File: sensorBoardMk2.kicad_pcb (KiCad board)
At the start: 2 copper layers, 47 parts, among them J1 B4B-PH-SM4-TB, J2 B4B-PH-SM4-TB, J3 B2B-PH-SM4-TB, J4 B2B-PH-SM4-TB, P1 TP, P2 TP, P3 TP, P4 TP, U1 SHT45, U2 BME280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

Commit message: Reworked schema
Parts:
- moved R5 2.97 mm to (91.2, 83.4)
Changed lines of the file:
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@@
 	(footprint "Resistor_SMD:R_0805_2012Metric_Pad1.20x1.40mm_HandSolder"
 		(layer "F.Cu")
-		(at 92.2 80.6)
+		(at 91.2 83.4)
 		(descr "Resistor SMD 0805 (2012 Metric), square (rectangular) end terminal, IPC-7351 nominal with elongated pad for handsoldering. (Body size source: IPC-SM-782 page 72, https://www.pcb-3d.com/wordpress/wp-content/uploads/ipc-sm-782a_amendment_1_and_2.pdf), generated with kicad-footprint-generator")
 		(tags "resistor handsolder")
@@
 		)
 		(fp_text user "${REFERENCE}"
-			(at 0 0 0)
+			(at -0.8 1.2 0)
 			(layer "F.Fab")
 			(effects

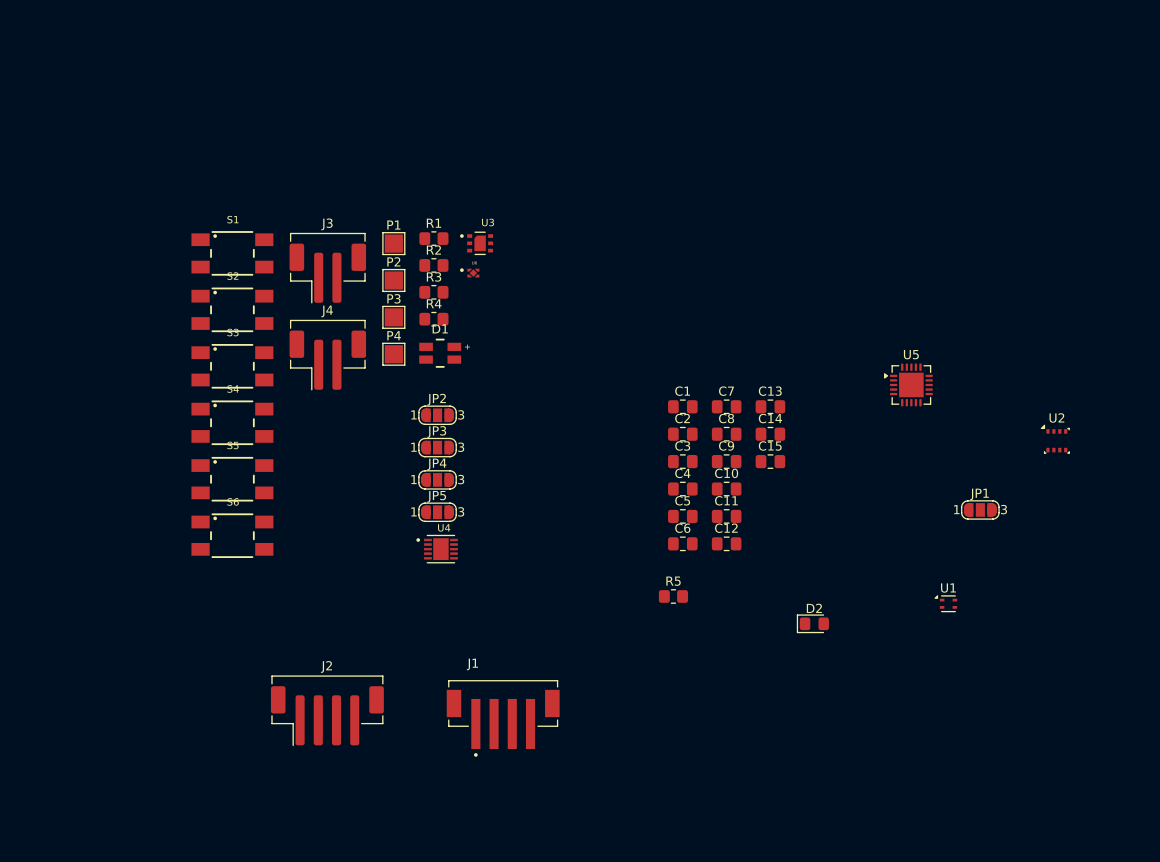
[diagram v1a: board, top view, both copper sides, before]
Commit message: Created pcb from schematic
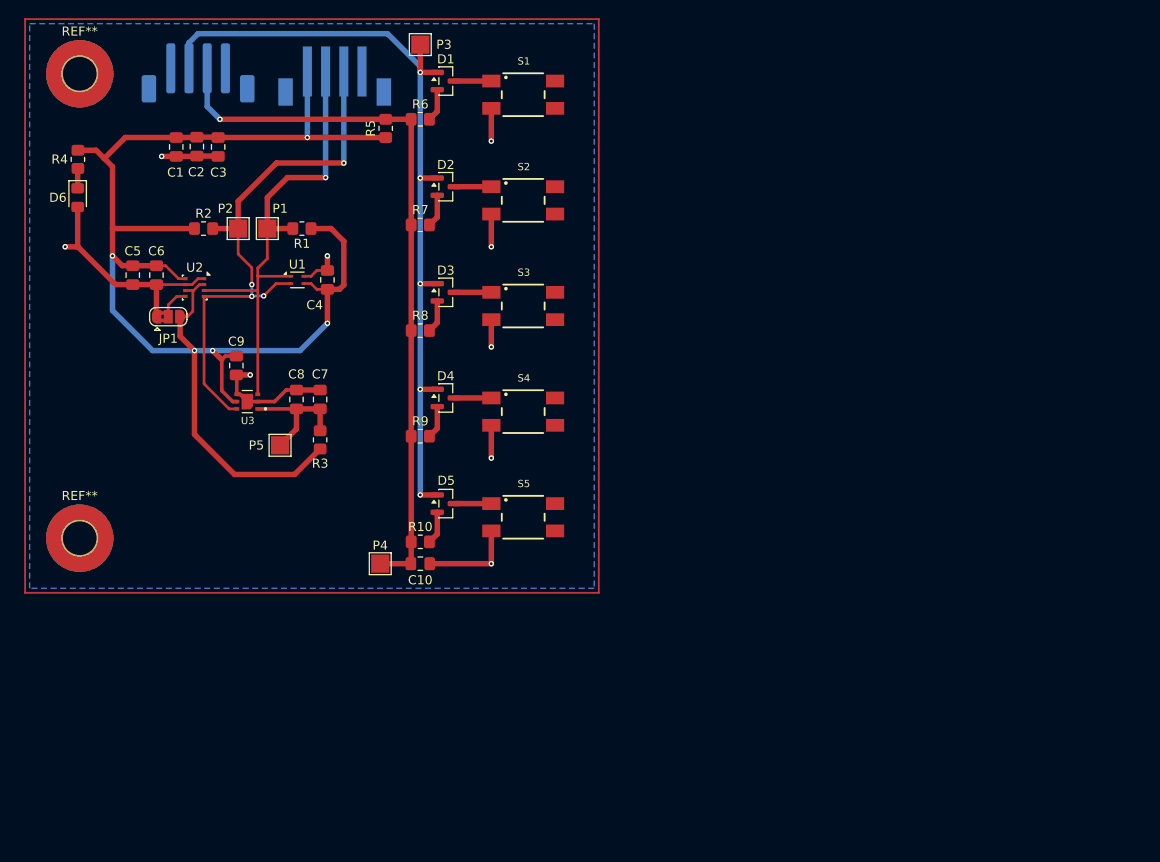
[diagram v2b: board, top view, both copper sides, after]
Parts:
- removed C11, C12, C14, C15: 1uF, Capacitor_SMD:C_0805_2012Metric_Pad1.18x1.45mm_HandSolder
- removed C13: 100nF, Capacitor_SMD:C_0805_2012Metric_Pad1.18x1.45mm_HandSolder
- removed J3, J4: B2B-PH-SM4-TB, Connector_JST:JST_PH_B2B-PH-SM4-TB_1x02-1MP_P2.00mm_Vertical
- removed JP2, JP3, JP4, JP5: SolderJumper_3_Bridged12, Jumper:SolderJumper-3_P1.3mm_Open_RoundedPad1.0x1.5mm_NumberLabels
- removed S6: 430181038816, sensorBoardMk2Library:430181038816
- removed U4: IS31FL3193-DLS2-TR, sensorBoardMk2Library:SON50P300X300X80-11N
- removed U5: MCP23008-xML, Package_DFN_QFN:QFN-20-1EP_4x4mm_P0.5mm_EP2.7x2.7mm
- removed U6: TPS7A0233PDQNR, sensorBoardMk2Library:IC_TPS7A0233PDQNR
- added D3: BAV70, Package_TO_SOT_SMD:SOT-23, F.Cu at (66.2, 50.0)
- added D4: BAV70, Package_TO_SOT_SMD:SOT-23, F.Cu at (66.2, 61.6)
- added D5: BAV70, Package_TO_SOT_SMD:SOT-23, F.Cu at (66.2, 73.2)
- added D6: LED_BLUE, LED_SMD:LED_0805_2012Metric_Pad1.15x1.40mm_HandSolder, F.Cu at (25.8, 39.6)
- added P5: TP, TestPoint:TestPoint_Pad_2.0x2.0mm, F.Cu at (48.0, 66.8)
- added R10: 56k, Resistor_SMD:R_0805_2012Metric_Pad1.20x1.40mm_HandSolder, F.Cu at (63.4, 77.4)
- added R6: 2.7k, Resistor_SMD:R_0805_2012Metric_Pad1.20x1.40mm_HandSolder, F.Cu at (63.4, 31.0)
- added R7: 5.6k, Resistor_SMD:R_0805_2012Metric_Pad1.20x1.40mm_HandSolder, F.Cu at (63.4, 42.6)
- added R8: 12k, Resistor_SMD:R_0805_2012Metric_Pad1.20x1.40mm_HandSolder, F.Cu at (63.4, 54.2)
- added R9: 22k, Resistor_SMD:R_0805_2012Metric_Pad1.20x1.40mm_HandSolder, F.Cu at (63.4, 65.8)
- added REF**: MountingHole_3.7mm_Pad_TopBottom, MountingHole:MountingHole_3.7mm_Pad_TopBottom, F.Cu at (26.0, 26.0)
- added REF**: MountingHole_3.7mm_Pad_TopBottom, MountingHole:MountingHole_3.7mm_Pad_TopBottom, F.Cu at (26.0, 77.0)
- D1: value WL-SFTW_3528_PLCC4 -> BAV70; footprint sensorBoardMk2Library:WL-SFTW_3528_PLCC4 -> Package_TO_SOT_SMD:SOT-23
- D2: value LED_RED -> BAV70; footprint LED_SMD:LED_0805_2012Metric_Pad1.15x1.40mm_HandSolder -> Package_TO_SOT_SMD:SOT-23
- J1, J2: moved to B.Cu
- JP1: footprint Jumper:SolderJumper-3_P1.3mm_Open_RoundedPad1.0x1.5mm_NumberLabels -> Jumper:SolderJumper-3_P1.3mm_Bridged2Bar12_RoundedPad1.0x1.5mm
- R1, R2: value 10k -> 5.6k
- R4: value 10k -> 120
- R5: value 2.7k -> 100k
- moved U2 96.2 mm to (38.6, 49.5), turned to -90 degrees
- moved JP1 91.7 mm to (35.7, 52.7)
- moved U1 79.9 mm to (49.9, 48.6)
- moved J2 72.0 mm to (39.0, 25.9)
- moved J1 69.7 mm to (54.0, 28.0)
- moved C5 66.0 mm to (31.8, 48.1), turned to -90 degrees
- moved C6 64.9 mm to (34.4, 48.1), turned to -90 degrees
- moved D2 62.8 mm to (66.2, 38.4)
- moved C1 62.5 mm to (36.6, 34.0), turned to -90 degrees
- moved C2 62.0 mm to (38.9, 34.0), turned to -90 degrees
- moved C3 61.6 mm to (41.2, 34.0), turned to -90 degrees
- moved R5 60.3 mm to (59.6, 32.0), turned to 90 degrees
- moved C9 54.9 mm to (43.2, 58.0), turned to -90 degrees
- moved C8 47.4 mm to (49.8, 61.8), turned to 90 degrees
- moved C4 45.3 mm to (53.2, 48.6), turned to 90 degrees
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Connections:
- C10 pad 1: /3V3_AO -> /ADC
- D1 pad 1: +3.3V -> /INT
- D1 pad 3: Net-(U4-OUT2) -> Net-(D1-K)
- D2 pad 1: Net-(D2-A) -> /INT
- D2 pad 2: GND -> Net-(D2-A-Pad2)
- J2 pad 2: /INT1 -> /INT
- J2 pad 3: /INT2 -> /ADC
- P3 pad 1: /INT1 -> /INT
- P4 pad 1: /INT2 -> /ADC
- R4 pad 1: /3V3_AO -> +3.3V
- R4 pad 2: /INT2 -> Net-(D6-A)
- R5 pad 1: /GP2 -> +3.3V
- R5 pad 2: Net-(D2-A) -> /ADC
- S1 pad 1: /INT2 -> Net-(D1-K)
- S1 pad 3: unconnected-(S1-Pad3) -> GND
- S1 pad 4: GND -> unconnected-(S1-Pad4)
- S2 pad 1: /GP3 -> Net-(D2-K)
- S2 pad 3: unconnected-(S2-Pad3) -> GND
- S2 pad 4: Net-(S2-Pad4) -> unconnected-(S2-Pad4)
- S3 pad 1: /GP4 -> Net-(D3-K)
- S3 pad 3: Net-(S2-Pad4) -> GND
- S3 pad 4: Net-(S3-Pad4) -> unconnected-(S3-Pad4)
- S4 pad 1: /GP5 -> Net-(D4-K)
- S4 pad 3: Net-(S3-Pad4) -> GND
- S4 pad 4: Net-(S4-Pad4) -> unconnected-(S4-Pad4)
- S5 pad 1: /GP6 -> Net-(D5-K)
- S5 pad 3: Net-(S4-Pad4) -> GND
- S5 pad 4: Net-(S5-Pad4) -> unconnected-(S5-Pad4)
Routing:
- net +3.3V: track 0.00 -> 167.1 mm, vias 0 -> 5
- net /INT: track 0.00 -> 89.5 mm, vias 0 -> 5
- net /ADC: track 0.00 -> 79.4 mm, vias 0 -> 1
- net GND: track 0.00 -> 73.7 mm, vias 0 -> 9
- net /SCL: track 0.00 -> 61.7 mm, vias 0 -> 4
- net /SDA: track 0.00 -> 53.4 mm, vias 0 -> 1
- net Net-(U3-VDD): track 0.00 -> 14.0 mm
- net Net-(D5-K): track 0.00 -> 4.06 mm
- net Net-(D4-K): track 0.00 -> 4.06 mm
- net Net-(D3-K): track 0.00 -> 4.06 mm
- net Net-(D2-K): track 0.00 -> 4.06 mm
- net Net-(D1-K): track 0.00 -> 4.06 mm
- net Net-(D4-A-Pad2): track 0.00 -> 3.62 mm
- net Net-(D1-A-Pad2): track 0.00 -> 3.62 mm
- net Net-(D3-A-Pad2): track 0.00 -> 3.62 mm
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- added copper zone on B.Cu, net GND

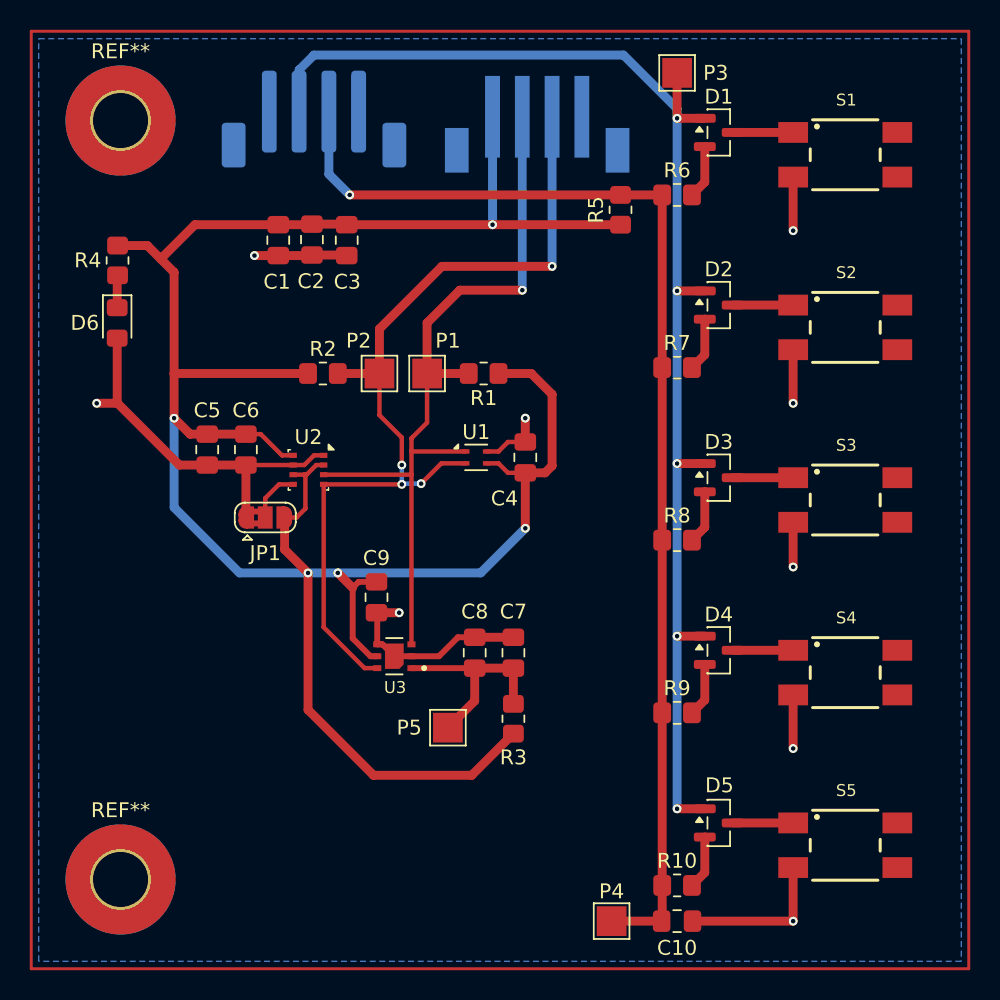
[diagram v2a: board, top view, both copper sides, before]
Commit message: Checked footprints of special parts
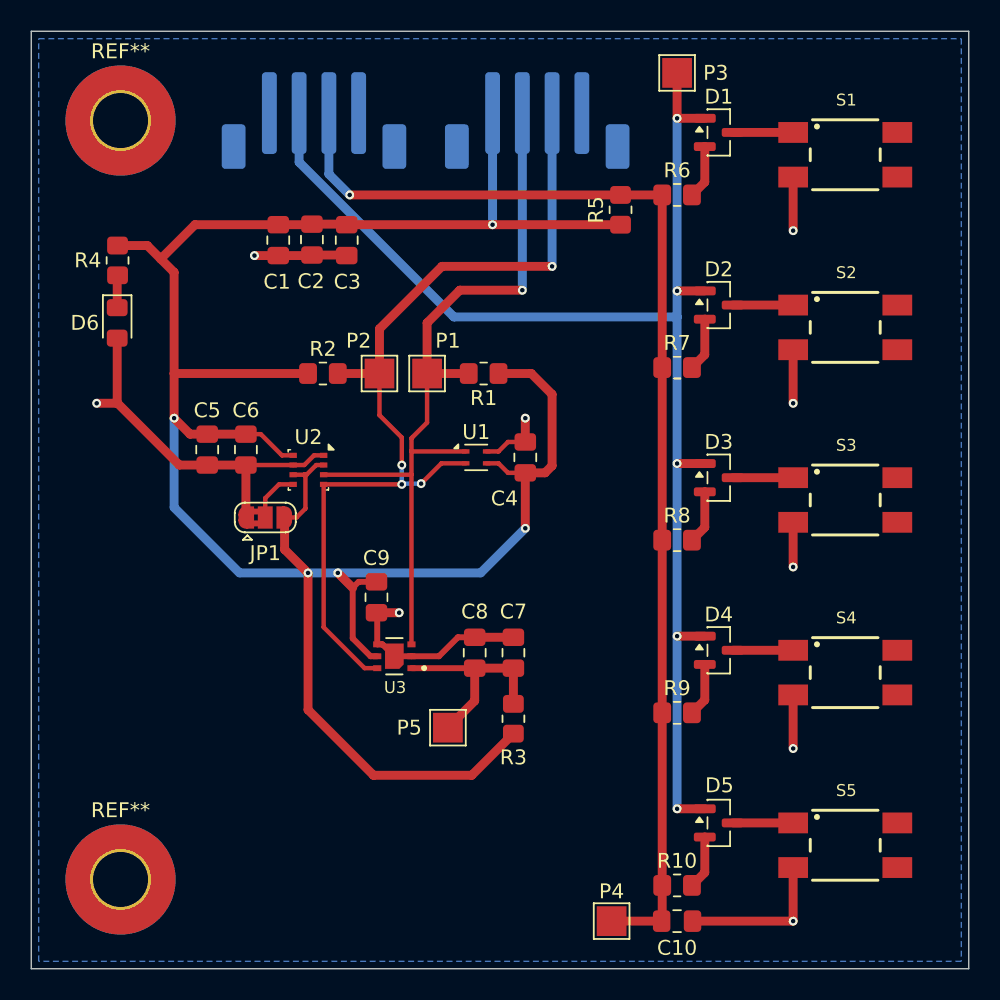
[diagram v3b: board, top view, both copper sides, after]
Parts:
- J1: footprint sensorBoardMk2Library:JST_B4B-PH-SM4-TB -> Connector_JST:JST_PH_B4B-PH-SM4-TB_1x04-1MP_P2.00mm_Vertical
- moved J1 2.00 mm to (54.0, 26.0)
- moved J2 0.10 mm to (39.0, 26.0)
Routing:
- net /INT: track 89.5 -> 91.8 mm
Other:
- board outline added: 63 x 63 mm

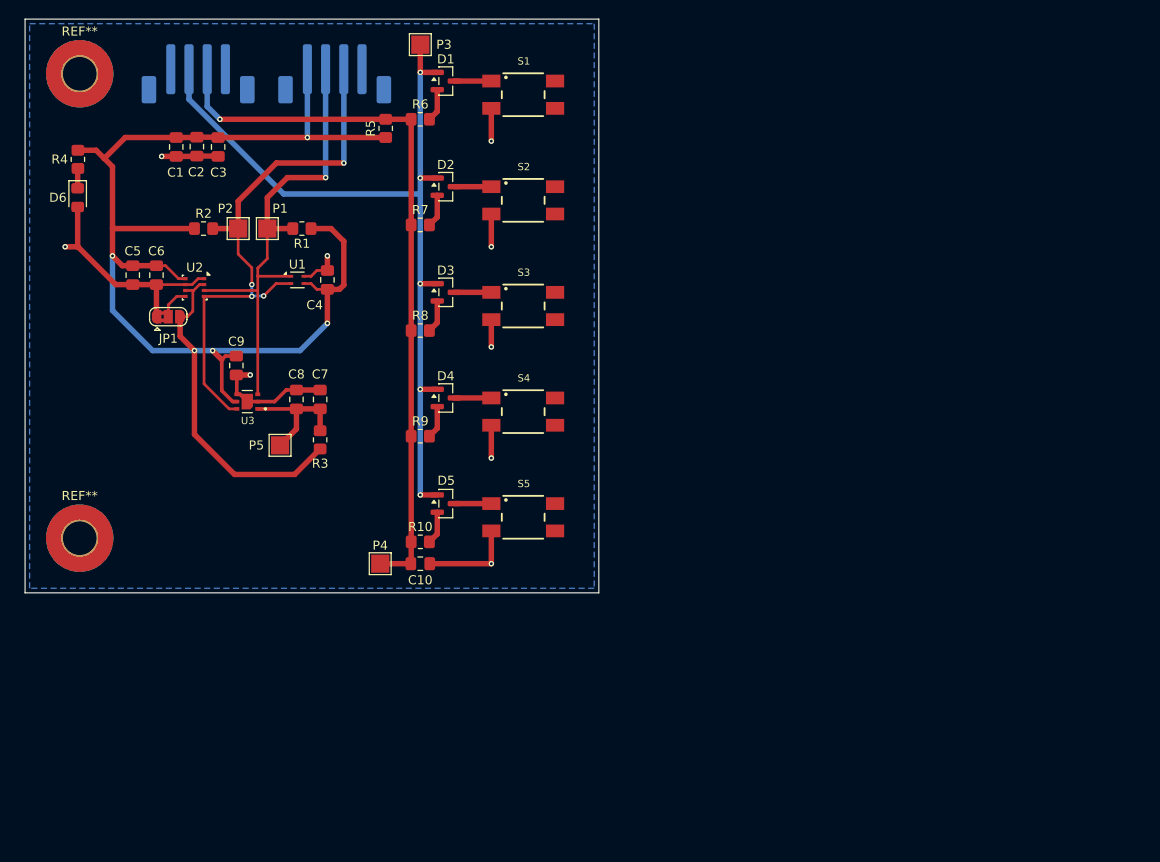
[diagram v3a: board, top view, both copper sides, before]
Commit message: Updated PCB to look cleaner, improved routing
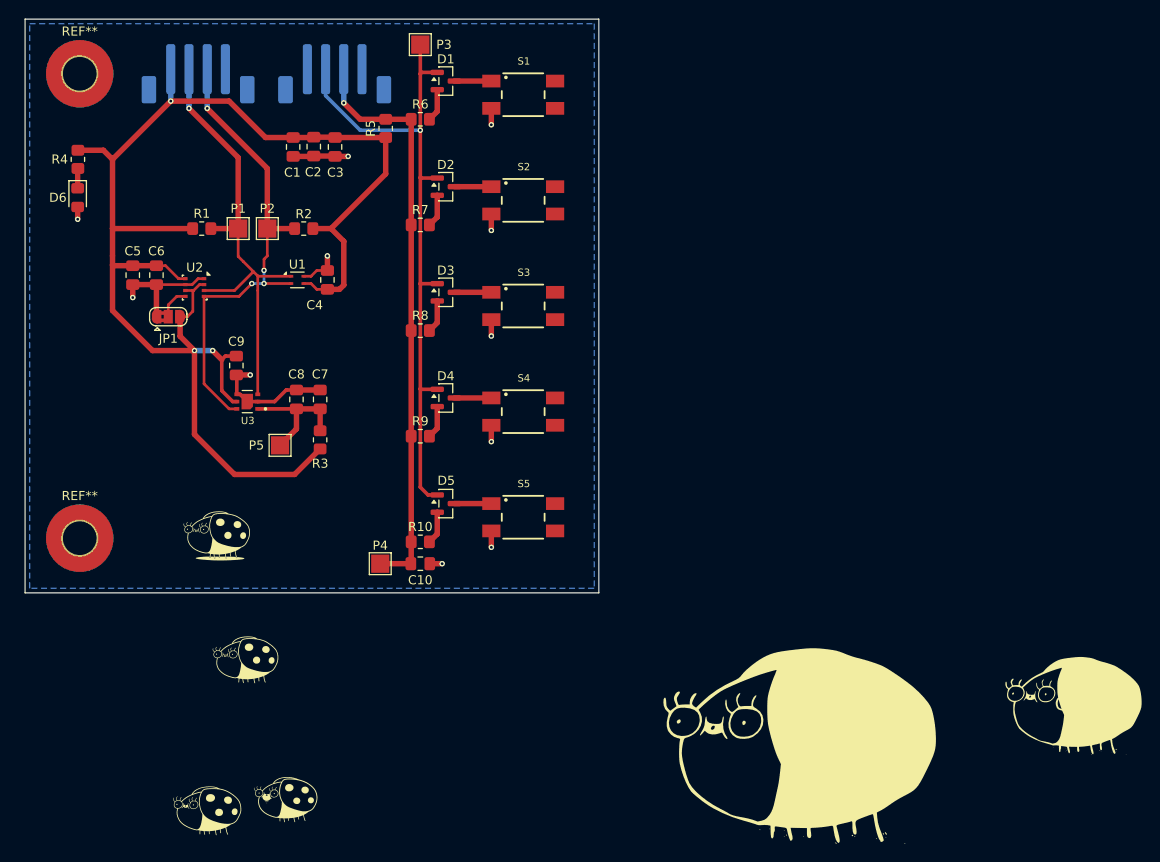
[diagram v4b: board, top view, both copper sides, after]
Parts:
- added G***: LOGO, LOGO, F.Cu at (44.2, 90.4)
- added G***: LOGO, LOGO, F.Cu at (41.0, 76.8)
- added G***: LOGO, LOGO, F.Cu at (105.6, 99.4)
- added G***: LOGO, LOGO, F.Cu at (48.6, 105.8)
- added G***: LOGO, LOGO, F.Cu at (40.0, 107.2)
- added G***: LOGO, LOGO, F.Cu at (135.4, 95.2)
- moved J1 15.0 mm to (39.0, 26.0)
- moved J2 15.0 mm to (54.0, 26.0)
- moved C2 12.8 mm to (51.7, 34.0)
- moved C1 12.8 mm to (49.4, 34.0)
- moved C3 12.8 mm to (54.0, 34.0)
- moved R1 11.0 mm to (39.4, 43.0), turned to 0 degrees
- moved R2 11.0 mm to (50.6, 43.0), turned to 180 degrees
- moved P1 3.20 mm to (43.4, 43.0)
- moved P2 3.20 mm to (46.6, 43.0)
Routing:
- net GND: track 73.7 -> 49.0 mm, vias 9 -> 11
- net /INT: track 91.8 -> 73.2 mm, vias 5 -> 1
- net /ADC: track 79.4 -> 64.0 mm
- net /SCL: track 61.7 -> 53.9 mm
- net +3.3V: track 167.1 -> 160.4 mm, vias 5 -> 3
- net /SDA: track 53.4 -> 51.8 mm

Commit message: Replaced the JST connectors with a THT connector, updated general schematics and checked the pinout on all connectors if they match to the LILYGO board
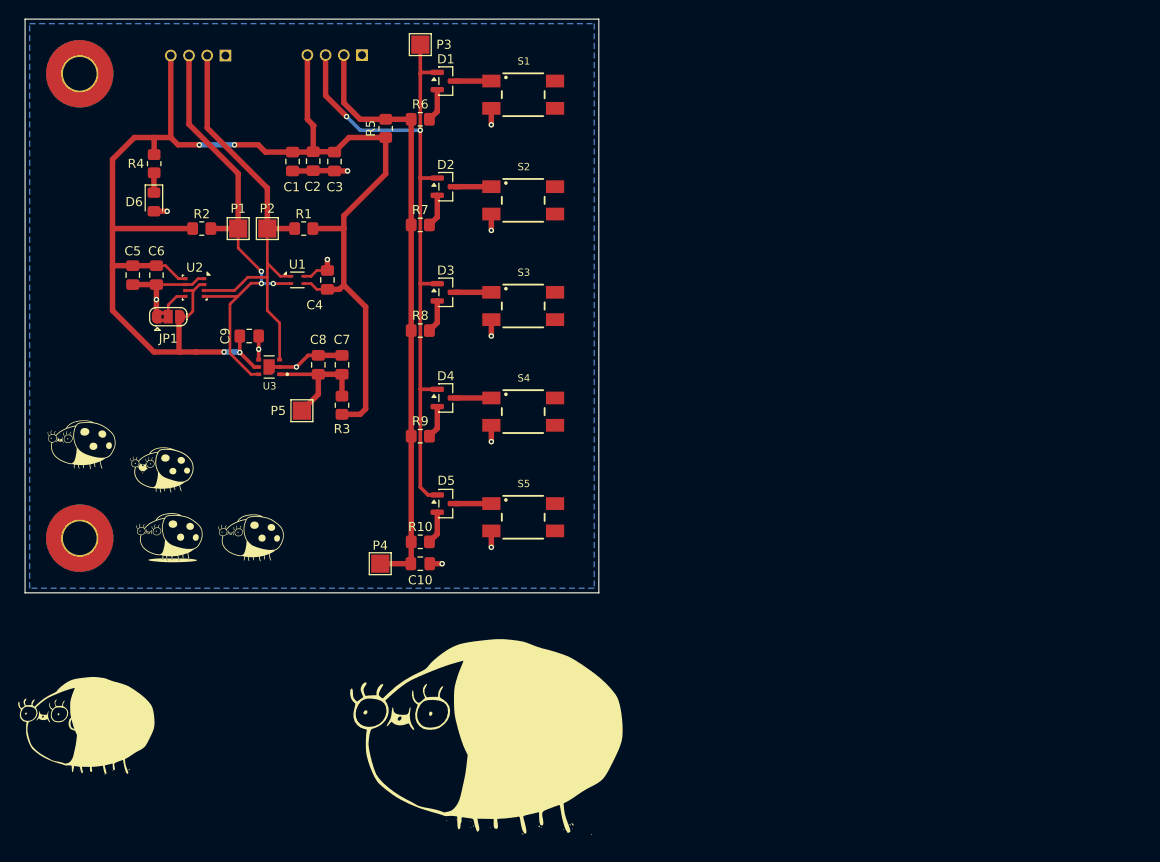
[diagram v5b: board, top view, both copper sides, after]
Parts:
- J1, J2: value B4B-PH-SM4-TB -> S4B-PH-K-S__LF__SN_; footprint Connector_JST:JST_PH_B4B-PH-SM4-TB_1x04-1MP_P2.00mm_Vertical -> JST-Connector-4_Pin_THT:JST_S4B-PH-K-S_LF__SN_
- moved G*** 108.4 mm to (27.0, 97.4)
- moved G*** 42.5 mm to (26.2, 67.0)
- moved G*** 38.7 mm to (35.0, 69.6)
- moved G*** 34.4 mm to (71.2, 98.4)
- moved G*** 13.4 mm to (44.8, 77.0)
- moved R1 11.2 mm to (50.6, 43.0), turned to 180 degrees
- moved R2 11.2 mm to (39.4, 43.0), turned to 0 degrees
- moved D6 8.39 mm to (34.1, 40.1)
- moved R4 8.39 mm to (34.2, 35.9)
- moved G*** 5.20 mm to (35.8, 77.0)
- moved C8 4.49 mm to (52.2, 58.0)
- moved C7 4.49 mm to (54.8, 58.0)
- moved R3 4.49 mm to (54.8, 62.4)
- moved P5 4.49 mm to (50.4, 63.0)
- moved U3 4.49 mm to (46.8, 58.2)
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- renumbered REF** to MountingHoleBottom, REF** to MountingHoleTop
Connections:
- J1 pad 1: +3.3V -> GND
- J1 pad 4: GND -> +3.3V
- J2 pad 1: unconnected-(J2-Pad1) -> GND
- J2 pad 2: /INT -> /ADC
- J2 pad 3: /ADC -> /INT
- J2 pad 4: unconnected-(J2-Pad4) -> +3.3V
- P1 pad 1: /SDA -> /SCL
- P2 pad 1: /SCL -> /SDA
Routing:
- net GND: track 49.0 -> 44.9 mm, vias 11 -> 12
- net /SCL: track 53.9 -> 50.8 mm, vias 4 -> 3
- net /SDA: track 51.8 -> 49.0 mm, vias 1 -> 0
- net +3.3V: track 160.4 -> 162.7 mm, vias 3 -> 4
- net /INT: track 73.2 -> 74.8 mm, vias 1 -> 2
- net /ADC: track 64.0 -> 65.6 mm, vias 1 -> 0
